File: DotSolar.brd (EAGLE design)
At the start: 25 x 35 mm, 19 parts, among them IC2 SI1145, Q1 BSH203, U1 ISL29125

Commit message: Update with exdended solar pad design
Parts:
- removed U$4: KXOB22-01X8F, IXYS_Solar_cells:KXOB22-01X8F
- added U$6: KXOB22-01X8F_EXTENDED_PADS, IXYS_Solar_cells:KXOB22-01X8F_EXTENDED_PADS
- U$1, U$2, U$3: value KXOB22-01X8F -> KXOB22-01X8F_EXTENDED_PADS; device IXYS_Solar_cells:KXOB22-01X8F -> IXYS_Solar_cells:KXOB22-01X8F_EXTENDED_PADS
- moved U$3 29.9 mm to (12.8, 31.4), turned to 90 degrees
- moved U$2 11.1 mm to (11.3, 15.0)
- moved U$1 10.9 mm to (18.6, 15.0)
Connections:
- net GND: now also U$6.P$1; no longer U$4.P$1
- net SOLAR_RAW: now also U$6.P$2; no longer U$4.P$2
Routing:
- net SOLAR_RAW: track 88.1 -> 86.7 mm
- net GND: track 91.3 -> 92.2 mm

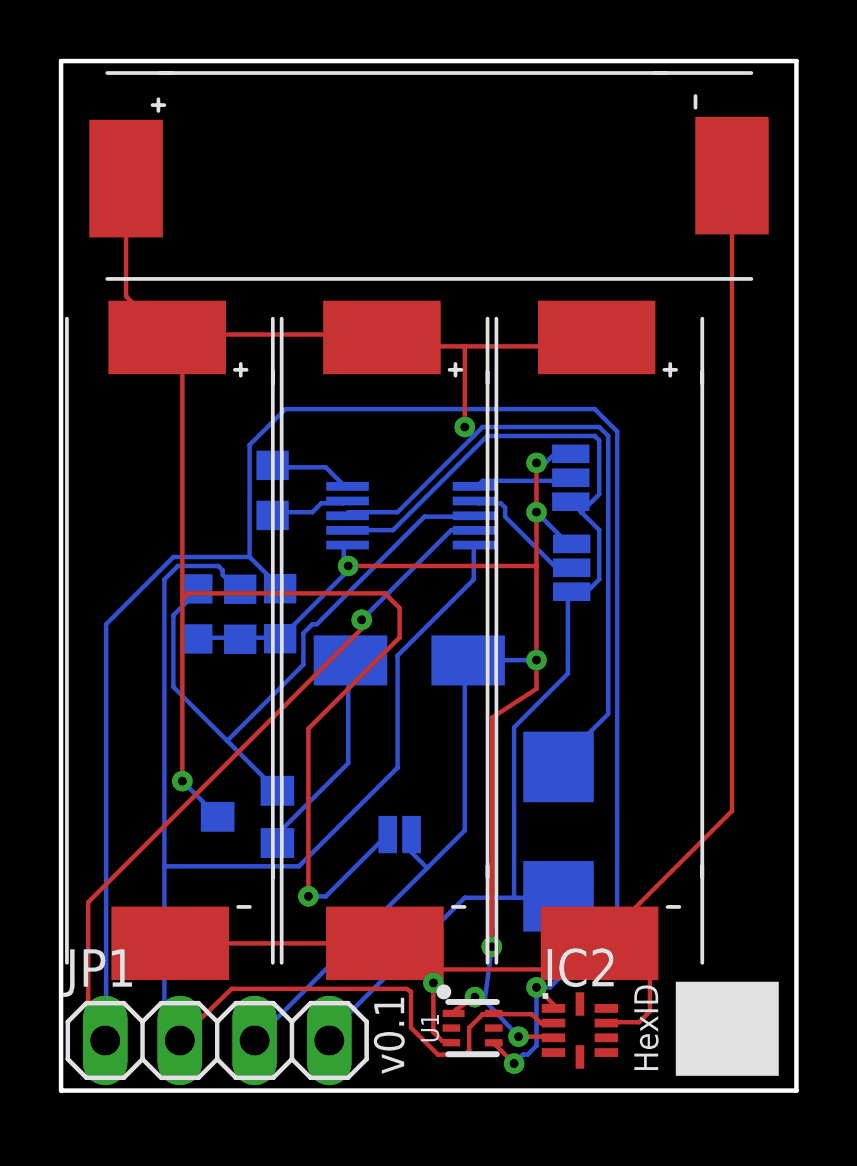
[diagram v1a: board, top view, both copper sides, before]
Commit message: Spacing cells further apart
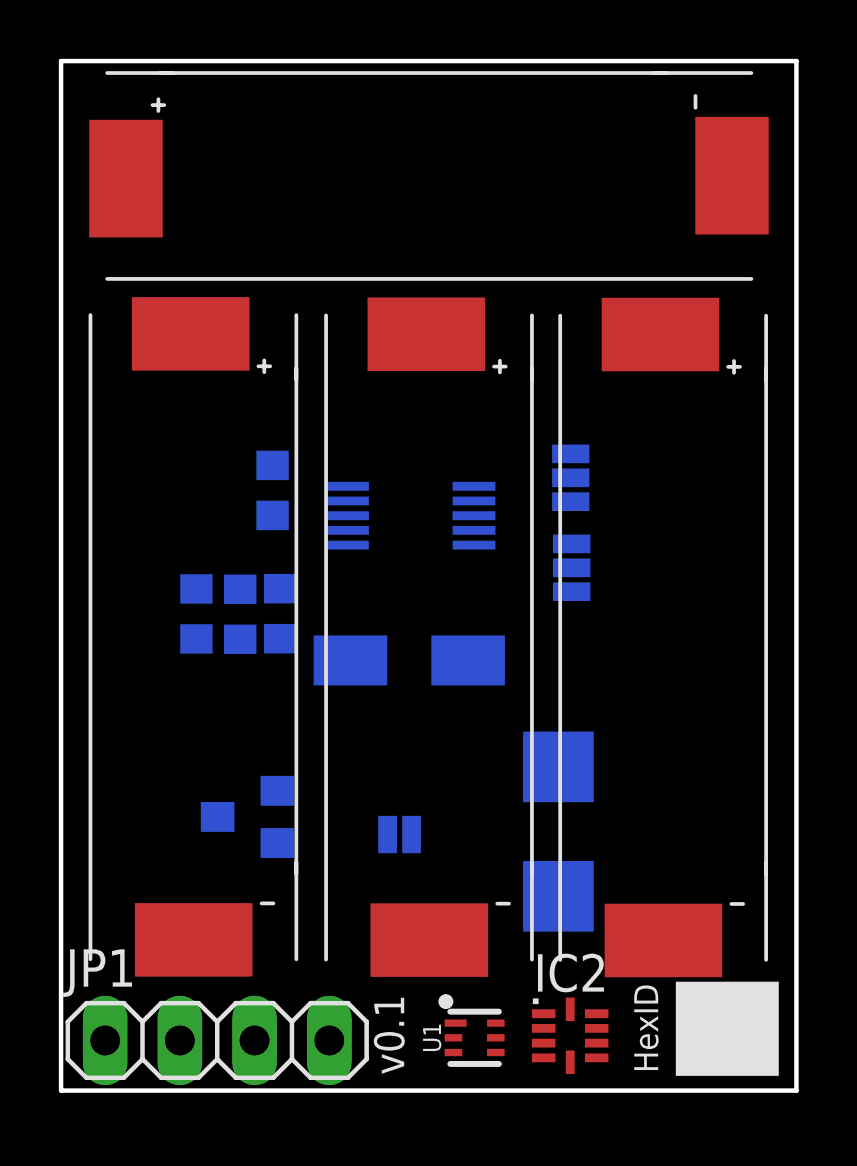
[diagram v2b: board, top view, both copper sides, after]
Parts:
- moved U$1 2.17 mm to (20.8, 15.1)
- moved U$2 1.51 mm to (12.8, 15.1)
- moved U$6 0.81 mm to (4.80, 15.1)
- moved IC2 0.38 mm to (17.3, 1.86)
- moved U1 0.34 mm to (14.1, 1.79)
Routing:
- net GND: track 92.2 -> 0.00 mm, vias 1 -> 0
- net SDA: track 87.4 -> 0.00 mm, vias 3 -> 0
- net SOLAR_RAW: track 86.7 -> 0.00 mm, vias 3 -> 0
- net 3V3: track 59.4 -> 0.00 mm, vias 7 -> 0
- net SCL: track 53.2 -> 0.00 mm
- net ALERT: track 20.8 -> 0.00 mm
- net N$1: track 7.22 -> 0.00 mm
- net A0: track 4.41 -> 0.00 mm
- net A1: track 3.40 -> 0.00 mm
- net IN+: track 2.82 -> 0.00 mm
- net IN-: track 2.74 -> 0.00 mm

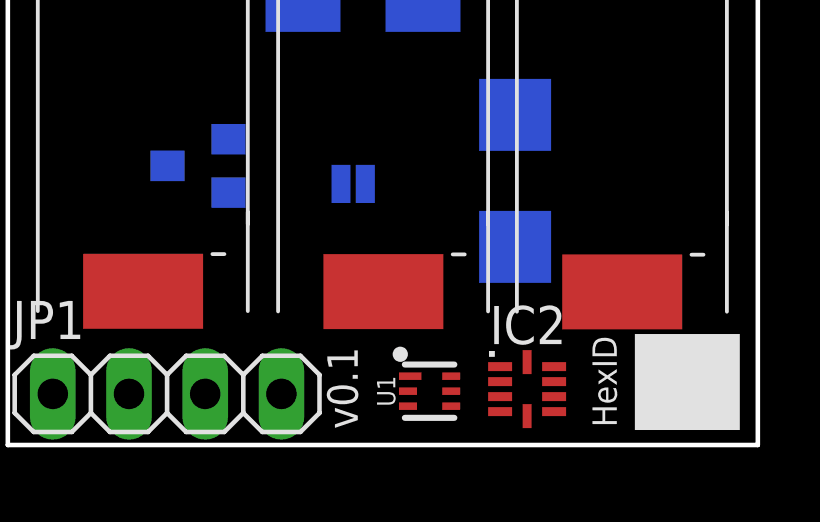
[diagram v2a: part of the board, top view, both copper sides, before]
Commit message: Add C1(10uF) and C2(1uF)
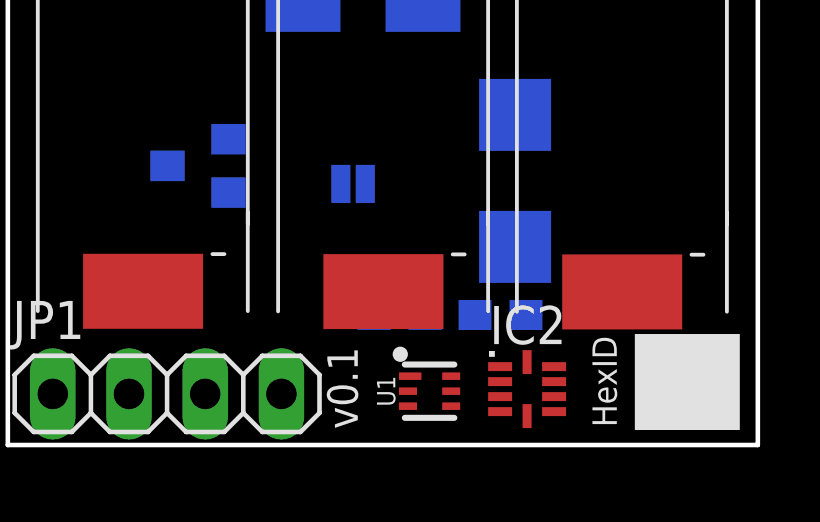
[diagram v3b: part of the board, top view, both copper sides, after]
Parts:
- added C1: 10uF, rcl:C0603
- added C2: 0.1uF, rcl:C0603
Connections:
- net 3V3: now also C1.1, C2.1
- net GND: now also C1.2, C2.2
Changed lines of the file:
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@@
 <layer number="20" name="Dimension" color="15" fill="1" visible="yes" active="yes"/>
 <layer number="21" name="tPlace" color="7" fill="1" visible="yes" active="yes"/>
-<layer number="22" name="bPlace" color="7" fill="1" visible="no" active="yes"/>
+<layer number="22" name="bPlace" color="7" fill="1" visible="yes" active="yes"/>
 <layer number="23" name="tOrigins" color="15" fill="1" visible="yes" active="yes"/>
-<layer number="24" name="bOrigins" color="15" fill="1" visible="no" active="yes"/>
+<layer number="24" name="bOrigins" color="15" fill="1" visible="yes" active="yes"/>
 <layer number="25" name="tNames" color="7" fill="1" visible="no" active="yes"/>
 <layer number="26" name="bNames" color="7" fill="1" visible="no" active="yes"/>
@@
 <element name="U$2" library="IXYS_Solar_cells" package="KXOB22-01X8F_EXTENDED_PADS" value="KXOB22-01X8F_EXTENDED_PADS" x="12.81" y="15.11"/>
 <element name="U$3" library="IXYS_Solar_cells" package="KXOB22-01X8F_EXTENDED_PADS" value="KXOB22-01X8F_EXTENDED_PADS" x="12.8" y="31.4" rot="R90"/>
+<element name="C1" library="rcl" package="C0603" value="10uF" x="16.41" y="4.33" rot="MR180"/>
+<element name="C2" library="rcl" package="C0603" value="0.1uF" x="13.05" y="4.33" rot="MR0"/>
 </elements>
 <signals>
@@
 <contactref element="U$2" pad="P$1"/>
 <contactref element="U$3" pad="P$1"/>
+<contactref element="C1" pad="2"/>
+<contactref element="C2" pad="2"/>
 <wire x1="17.32" y1="20.0172" x2="22.8" y2="31.1" width="0" layer="19" extent="1-16"/>
 <wire x1="17.35" y1="16.9572" x2="17.32" y2="20.0172" width="0" layer="19" extent="16-16"/>
@@
 <wire x1="20.47" y1="5.1" x2="16.9" y2="6.6" width="0" layer="19" extent="1-16"/>
 <wire x1="18.2" y1="2.11" x2="20.47" y2="5.1" width="0" layer="19" extent="1-1"/>
-<wire x1="13.33" y1="1.29" x2="18.2" y2="2.11" width="0" layer="19" extent="1-1"/>
-<wire x1="12.51" y1="5.11" x2="13.33" y2="1.29" width="0" layer="19" extent="1-1"/>
-<wire x1="9.11" y1="1.7" x2="12.51" y2="5.11" width="0" layer="19" extent="1-1"/>
+<wire x1="12.51" y1="5.11" x2="16.9" y2="6.6" width="0" layer="19" extent="1-16"/>
+<wire x1="13.33" y1="1.29" x2="12.51" y2="5.11" width="0" layer="19" extent="1-1"/>
+<wire x1="9.11" y1="1.7" x2="13.33" y2="1.29" width="0" layer="19" extent="1-1"/>
 <wire x1="4.5" y1="5.12" x2="9.11" y2="1.7" width="0" layer="19" extent="1-1"/>
+<wire x1="17.26" y1="4.33" x2="17.35" y2="16.9572" width="0" layer="19" extent="16-16"/>
+<wire x1="12.2" y1="4.33" x2="9.11" y2="1.7" width="0" layer="19" extent="1-1"/>
 </signal>
 <signal name="3V3">
@@
 <contactref element="D1" pad="CATHODE"/>
 <contactref element="JP2" pad="2"/>
-<wire x1="17.35" y1="18.5828" x2="17.32" y2="21.6428" width="0" layer="19" extent="16-16"/>
+<contactref element="C2" pad="1"/>
+<contactref element="C1" pad="1"/>
+<wire x1="17.35" y1="18.5828" x2="15.56" y2="4.33" width="0" layer="19" extent="16-16"/>
+<wire x1="17.32" y1="21.6428" x2="17.35" y2="18.5828" width="0" layer="19" extent="16-16"/>
 <wire x1="13.83" y1="14.62" x2="17.35" y2="18.5828" width="0" layer="19" extent="16-16"/>
 <wire x1="9.73" y1="18.54" x2="13.83" y2="14.62" width="0" layer="19" extent="16-16"/>
@@
 <wire x1="16.4" y1="1.61" x2="13.405" y2="2.29" width="0" layer="19" extent="1-1"/>
 <wire x1="6.57" y1="1.7" x2="13.405" y2="2.29" width="0" layer="19" extent="1-1"/>
+<wire x1="13.9" y1="4.33" x2="6.57" y2="1.7" width="0" layer="19" extent="1-1"/>
 </signal>
 <signal name="A0">
@@
 <contactref element="U$5" pad="4"/>
 <wire x1="7.44" y1="17.06" x2="14.03" y2="19.04" width="0" layer="19" extent="16-16"/>
-<wire x1="16.4" y1="2.61" x2="14.03" y2="19.04" width="0" layer="19" extent="1-16"/>
-<wire x1="14.77" y1="1.29" x2="16.4" y2="2.61" width="0" layer="19" extent="1-1"/>
-<wire x1="1.49" y1="1.7" x2="14.77" y2="1.29" width="0" layer="19" extent="1-1"/>
+<wire x1="1.49" y1="1.7" x2="7.44" y2="17.06" width="0" layer="19" extent="16-16"/>
+<wire x1="14.77" y1="1.29" x2="1.49" y2="1.7" width="0" layer="19" extent="1-1"/>
+<wire x1="16.4" y1="2.61" x2="14.77" y2="1.29" width="0" layer="19" extent="1-1"/>
 </signal>
 <signal name="SCL">

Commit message: Add GND planes
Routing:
- net SCL: track 0.00 -> 94.0 mm, vias 0 -> 3
- net GND: track 0.00 -> 94.0 mm, vias 0 -> 66
- net SDA: track 0.00 -> 69.9 mm, vias 0 -> 4
- net 3V3: track 0.00 -> 65.2 mm, vias 0 -> 6
- net SOLAR_RAW: track 0.00 -> 63.4 mm, vias 0 -> 4
- net ALERT: track 0.00 -> 20.2 mm
- net N$1: track 0.00 -> 7.22 mm
- net A0: track 0.00 -> 4.41 mm
- net A1: track 0.00 -> 3.40 mm
- net IN+: track 0.00 -> 2.82 mm
- net IN-: track 0.00 -> 2.74 mm
- added copper zone on layer 1, net GND
- added copper zone on layer 16, net GND
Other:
- board text added: "First solder the light sensors"

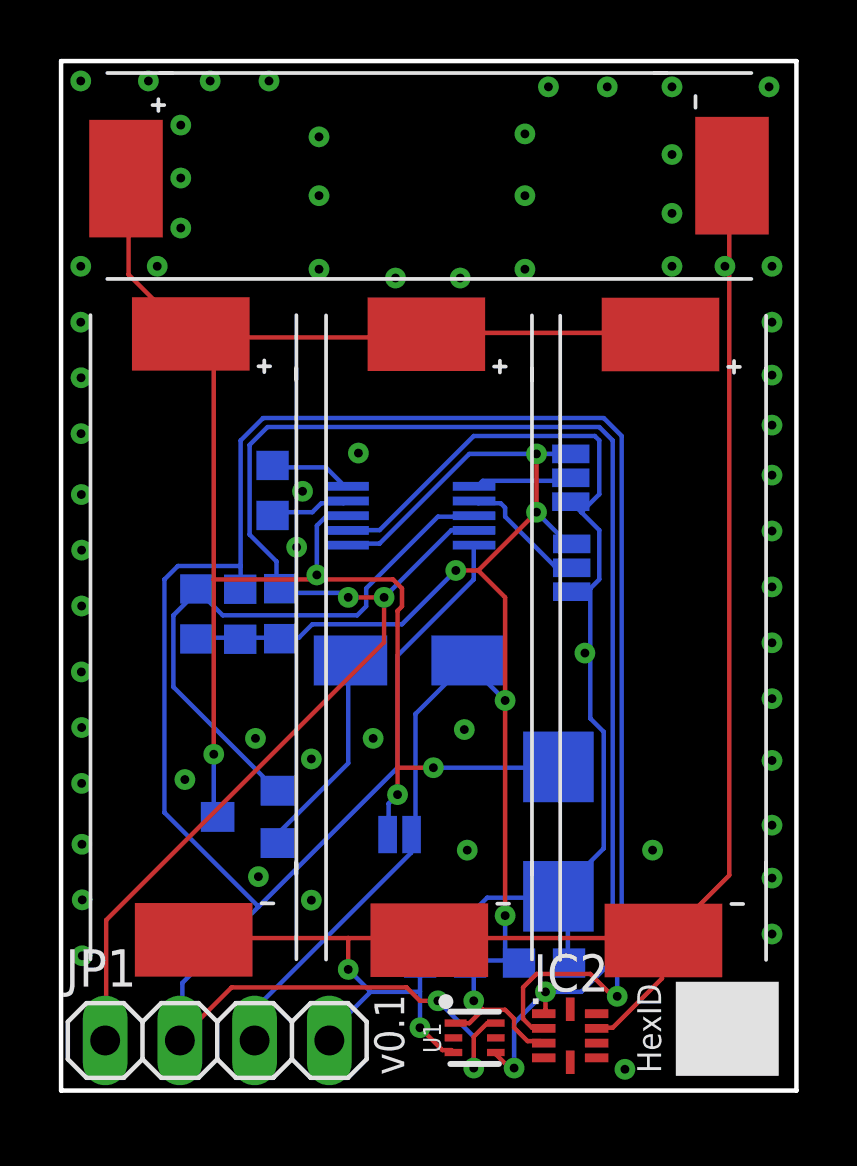
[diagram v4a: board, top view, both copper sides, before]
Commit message: Add CAT24M01 8Mbit EEPROM
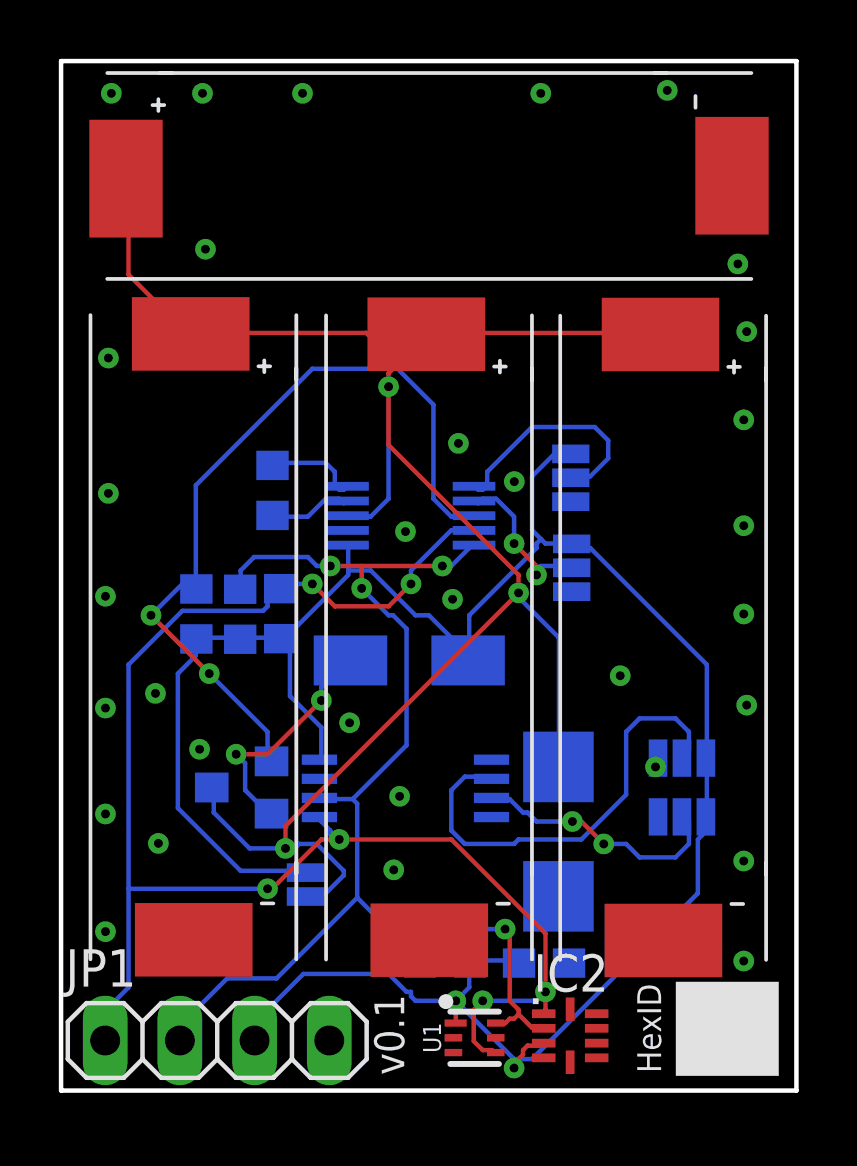
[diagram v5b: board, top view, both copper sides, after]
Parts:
- added IC1: CAT24M010TS, CAT24M01YI:TSSOP8
- added SJ1, SJ4: (no value), SparkFun:SJ_3_PASTE2&3
- moved JP2 3.62 mm to (8.30, 7.00), turned to 90 degrees
- moved Q1 1.02 mm to (6.13, 10.3)
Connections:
- new net EEPROM_A1: IC1.A1, SJ1.2
- new net EEPROM_A2: IC1.A2, SJ4.2
- net 3V3: now also IC1.VCC, SJ1.3, SJ4.3
- net GND: now also IC1.GND, IC1.NC, SJ1.1, SJ4.1
- net SCL: now also IC1.SCL
- net SDA: now also IC1.SDA
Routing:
- net GND: track 94.0 -> 0.00 mm, vias 66 -> 32
- net SCL: track 94.0 -> 42.1 mm, vias 3 -> 4
- net SDA: track 69.9 -> 52.4 mm, vias 4 -> 6
- net EEPROM_A1: track 0.00 -> 15.4 mm
- net 3V3: track 65.2 -> 79.3 mm, vias 6 -> 2
- net EEPROM_A2: track 0.00 -> 8.82 mm, vias 0 -> 2
- net ALERT: track 20.2 -> 27.4 mm, vias 0 -> 2
- net A1: track 3.40 -> 8.10 mm
- net SOLAR_RAW: track 63.4 -> 66.2 mm, vias 4 -> 3
- net A0: track 4.41 -> 5.42 mm, vias 0 -> 2
- net N$1: track 7.22 -> 8.04 mm, vias 0 -> 2
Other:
- board text added: "Current Sense"
- board text added: "EEPROM"

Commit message: EEPROM default address 0x52 and 0x53
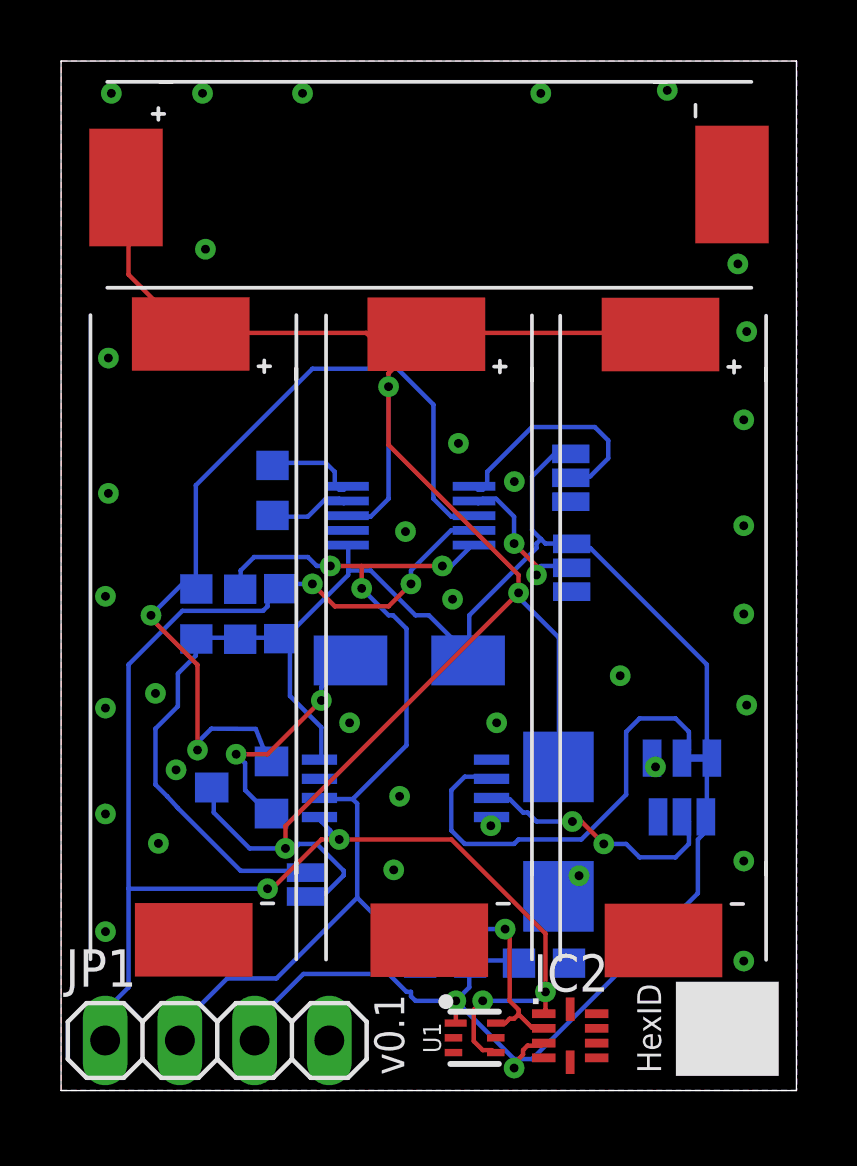
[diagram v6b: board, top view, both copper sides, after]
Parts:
- removed SJ1: (no value), SparkFun:SJ_3_PASTE2&3
- added JP3: JUMPER-SMT_3_1-NC_TRACE_SILK, SparkFun-Jumpers:SMT-JUMPER_3_1-NC_TRACE_SILK
- moved U$3 0.30 mm to (12.8, 31.1)
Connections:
- net 3V3: now also JP3.3; no longer SJ1.3
- net EEPROM_A1: now also JP3.2; no longer SJ1.2
- net GND: now also JP3.1; no longer SJ1.1
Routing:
- net ALERT: track 27.4 -> 29.7 mm
- net GND: track 0.00 -> 0.32 mm, vias 32 -> 35
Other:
- board text added: "A2"
